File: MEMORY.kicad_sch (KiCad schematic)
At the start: 5 parts, among them U2 ICE40HX8K-BG121, U7 S27KL0641

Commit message: Routing changes, pullups, etc
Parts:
- C21, C22, C26, U2: Source (none) -> ANY
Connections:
- net ~CS1: now also U2.D10 (IOR_154); no longer U2.B11 (IOR_161)
- net ~RESET1: now also U2.B11 (IOR_161); no longer U2.D10 (IOR_154)

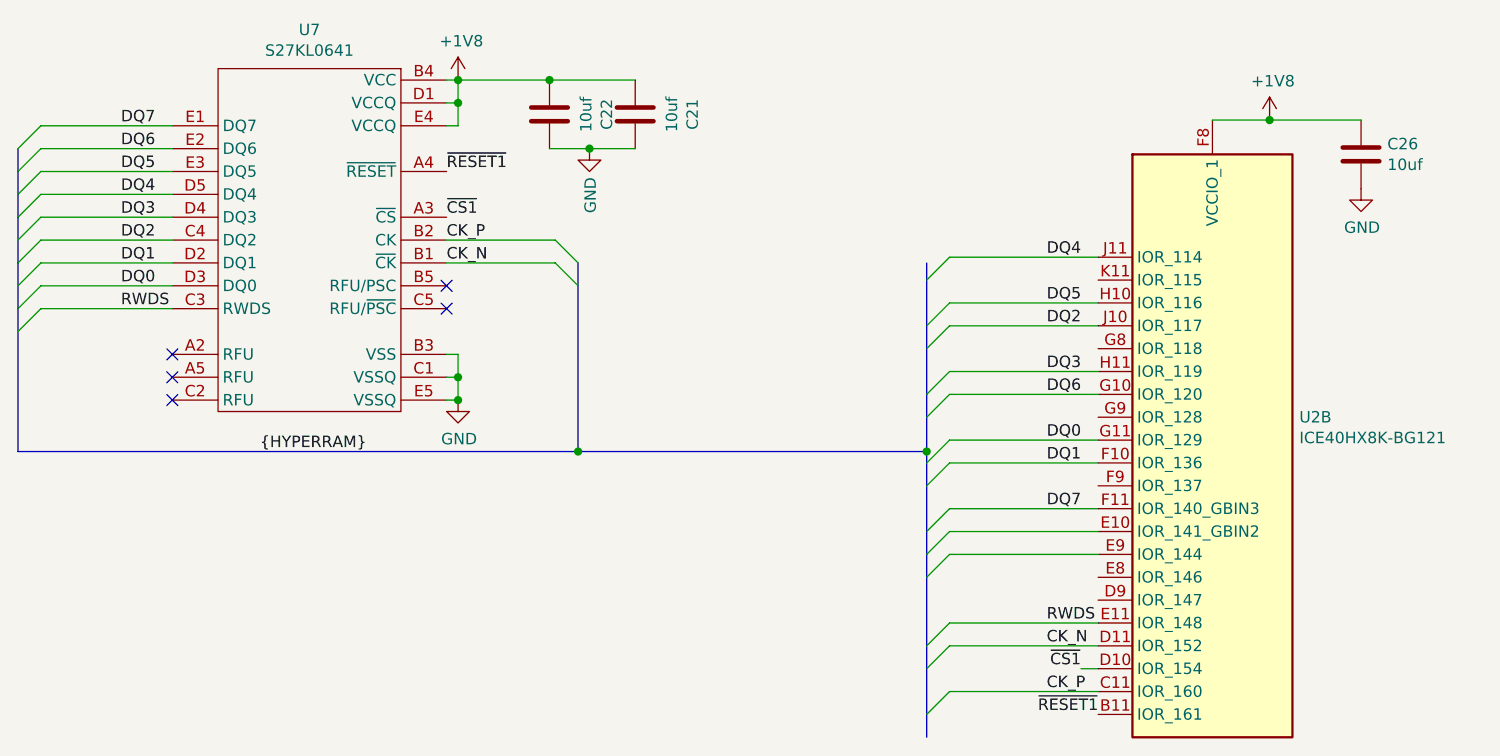
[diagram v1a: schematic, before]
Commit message: Routing cleanup, fix primary transformer
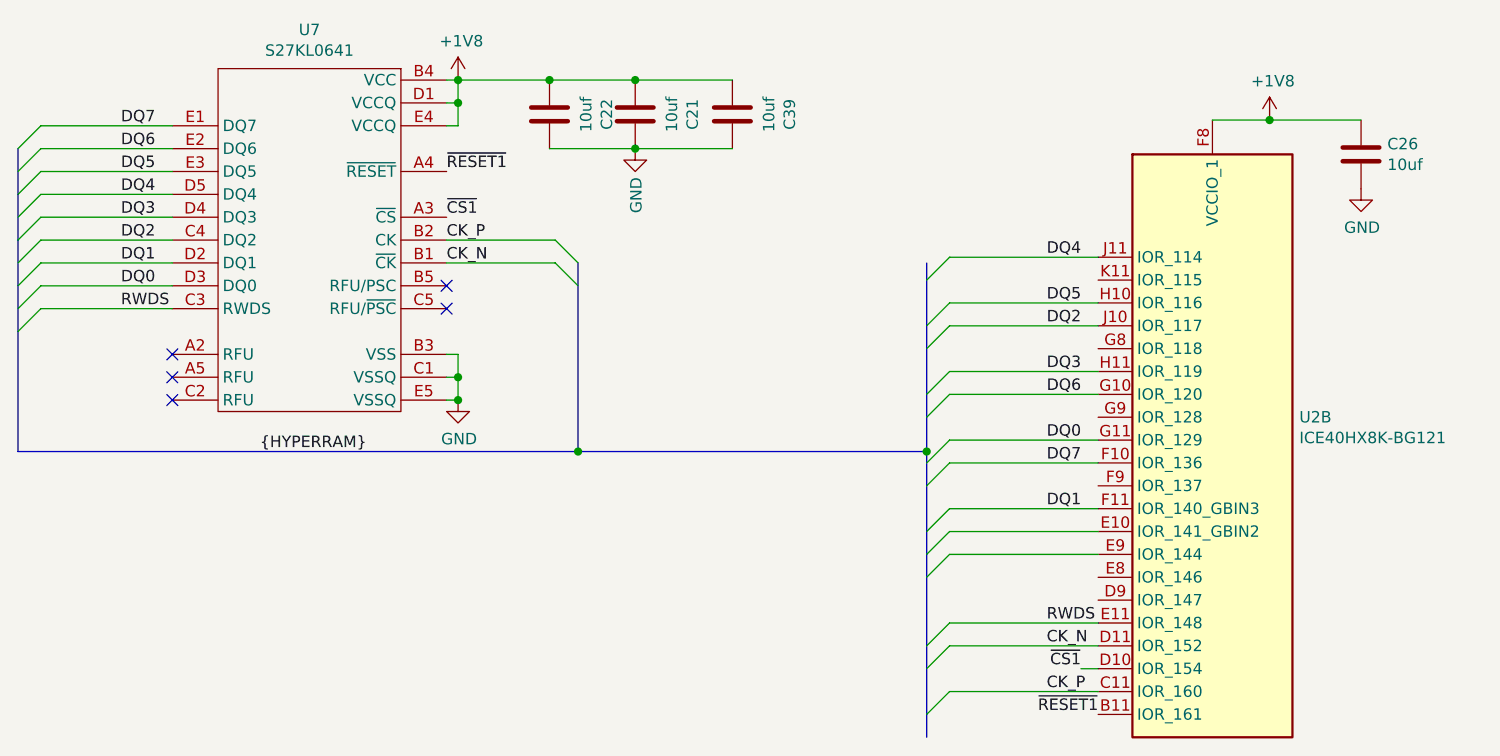
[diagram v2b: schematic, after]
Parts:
- added C39: 10uf, Capacitor_SMD:C_0402_1005Metric, symbol Device:C
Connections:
- net +1V8: now also C39.1
- net DQ1: now also U2.F11 (IOR_140_GBIN3); no longer U2.F10 (IOR_136)
- net DQ7: now also U2.F10 (IOR_136); no longer U2.F11 (IOR_140_GBIN3)
- net GND: now also C39.2
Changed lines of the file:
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@@
   (page 5 7)
   (paper "A4")
+  (title_block
+    (rev "TEST")
+  )
   (bus_alias "HYPERRAM" (members "DQ[7..0]" "RWDS" "~CS" "CK" "~CK" "RFU/PSC" "RFU/~PSC"))
   (junction (at 118.745 57.785))
@@
   (junction (at 118.745 93.345))
   (junction (at 128.905 57.785))
-  (junction (at 133.35 65.405))
+  (junction (at 138.43 57.785))
+  (junction (at 138.43 65.405))
   (junction (at 208.915 62.23))
   (junction (at 132.08 99.06))
   (junction (at 170.815 99.06))
   (no_connect (at 117.475 80.645))
-  (no_connect (at 86.995 90.805))
+  (no_connect (at 86.995 93.345))
   (no_connect (at 117.475 83.185))
   (no_connect (at 86.995 88.265))
-  (no_connect (at 86.995 93.345))
+  (no_connect (at 86.995 90.805))
   (bus_entry (at 69.85 65.405) (size 2.54 -2.54))
   (bus_entry (at 69.85 67.945) (size 2.54 -2.54))
@@
     (stroke (width 0) (type solid) (color 0 0 0 0))
   )
-  (wire (pts (xy 128.905 65.405) (xy 133.35 65.405))
-    (stroke (width 0) (type solid) (color 0 0 0 0))
-  )
-  (wire (pts (xy 133.35 65.405) (xy 138.43 65.405))
+  (wire (pts (xy 128.905 65.405) (xy 138.43 65.405))
+    (stroke (width 0) (type solid) (color 0 0 0 0))
+  )
+  (wire (pts (xy 138.43 57.785) (xy 149.225 57.785))
+    (stroke (width 0) (type solid) (color 0 0 0 0))
+  )
+  (wire (pts (xy 138.43 65.405) (xy 149.225 65.405))
     (stroke (width 0) (type solid) (color 0 0 0 0))
   )
@@
     (stroke (width 0) (type solid) (color 0 0 0 0))
   )
-  (bus (pts (xy 69.85 65.405) (xy 69.85 67.945))
-    (stroke (width 0) (type solid) (color 0 0 0 0))
-  )
-  (bus (pts (xy 69.85 67.945) (xy 69.85 73.025))
-    (stroke (width 0) (type solid) (color 0 0 0 0))
-  )
-  (bus (pts (xy 69.85 73.025) (xy 69.85 78.105))
-    (stroke (width 0) (type solid) (color 0 0 0 0))
-  )
-  (bus (pts (xy 69.85 78.105) (xy 69.85 83.185))
-    (stroke (width 0) (type solid) (color 0 0 0 0))
-  )
-  (bus (pts (xy 69.85 83.185) (xy 69.85 99.06))
+  (bus (pts (xy 69.85 65.405) (xy 69.85 70.485))
+    (stroke (width 0) (type solid) (color 0 0 0 0))
+  )
+  (bus (pts (xy 69.85 70.485) (xy 69.85 75.565))
+    (stroke (width 0) (type solid) (color 0 0 0 0))
+  )
+  (bus (pts (xy 69.85 75.565) (xy 69.85 80.645))
+    (stroke (width 0) (type solid) (color 0 0 0 0))
+  )
+  (bus (pts (xy 69.85 80.645) (xy 69.85 85.725))
+    (stroke (width 0) (type solid) (color 0 0 0 0))
+  )
+  (bus (pts (xy 69.85 85.725) (xy 69.85 99.06))
     (stroke (width 0) (type solid) (color 0 0 0 0))
   )
@@
     (stroke (width 0) (type solid) (color 0 0 0 0))
   )
-  (bus (pts (xy 170.815 85.09) (xy 170.815 92.71))
-    (stroke (width 0) (type solid) (color 0 0 0 0))
-  )
-  (bus (pts (xy 170.815 92.71) (xy 170.815 99.06))
+  (bus (pts (xy 170.815 85.09) (xy 170.815 87.63))
+    (stroke (width 0) (type solid) (color 0 0 0 0))
+  )
+  (bus (pts (xy 170.815 87.63) (xy 170.815 95.25))
+    (stroke (width 0) (type solid) (color 0 0 0 0))
+  )
+  (bus (pts (xy 170.815 95.25) (xy 170.815 99.06))
     (stroke (width 0) (type solid) (color 0 0 0 0))
   )
@@
     (stroke (width 0) (type solid) (color 0 0 0 0))
   )
-  (bus (pts (xy 170.815 110.49) (xy 170.815 113.03))
-    (stroke (width 0) (type solid) (color 0 0 0 0))
-  )
-  (bus (pts (xy 170.815 113.03) (xy 170.815 123.19))
-    (stroke (width 0) (type solid) (color 0 0 0 0))
-  )
-  (bus (pts (xy 170.815 123.19) (xy 170.815 130.81))
+  (bus (pts (xy 170.815 110.49) (xy 170.815 120.65))
+    (stroke (width 0) (type solid) (color 0 0 0 0))
+  )
+  (bus (pts (xy 170.815 120.65) (xy 170.815 128.27))
+    (stroke (width 0) (type solid) (color 0 0 0 0))
+  )
+  (bus (pts (xy 170.815 128.27) (xy 170.815 130.81))
     (stroke (width 0) (type solid) (color 0 0 0 0))
   )
@@
     (effects (font (size 1.27 1.27)) (justify left bottom))
   )
-  (label "DQ1" (at 184.15 100.33 0)
-    (effects (font (size 1.27 1.27)) (justify left bottom))
-  )
-  (label "DQ7" (at 184.15 105.41 0)
+  (label "DQ7" (at 184.15 100.33 0)
+    (effects (font (size 1.27 1.27)) (justify left bottom))
+  )
+  (label "DQ1" (at 184.15 105.41 0)
     (effects (font (size 1.27 1.27)) (justify left bottom))
   )
@@
     )
   )
-  (symbol (lib_id "power:GND") (at 133.35 65.405 0) (unit 1)
-    (property "Reference" "#PWR0148" (id 0) (at 133.35 71.755 0)
-      (effects (font (size 1.27 1.27)) hide)
-    )
-    (property "Value" "GND" (id 1) (at 133.4643 68.5801 90)
+  (symbol (lib_id "power:GND") (at 138.43 65.405 0) (unit 1)
+    (property "Reference" "#PWR0148" (id 0) (at 138.43 71.755 0)
+      (effects (font (size 1.27 1.27)) hide)
+    )
+    (property "Value" "GND" (id 1) (at 138.5443 68.5801 90)
       (effects (font (size 1.27 1.27)) (justify right))
     )
-    (property "Footprint" "" (id 2) (at 133.35 65.405 0)
-      (effects (font (size 1.27 1.27)) hide)
-    )
-    (property "Datasheet" "" (id 3) (at 133.35 65.405 0)
+    (property "Footprint" "" (id 2) (at 138.43 65.405 0)
+      (effects (font (size 1.27 1.27)) hide)
+    )
+    (property "Datasheet" "" (id 3) (at 138.43 65.405 0)
       (effects (font (size 1.27 1.27)) hide)
     )
@@
       (effects (font (size 1.27 1.27)) hide)
     )
+  )
+  (symbol (lib_id "Device:C") (at 149.225 61.595 0) (unit 1)
+    (property "Reference" "C39" (id 0) (at 155.5942 61.595 90))
+    (property "Value" "10uf" (id 1) (at 153.2955 61.595 90))
+    (property "Footprint" "Capacitor_SMD:C_0402_1005Metric" (id 2) (at 150.1902 65.405 0)
+      (effects (font (size 1.27 1.27)) hide)
+    )
+    (property "Datasheet" "~" (id 3) (at 149.225 61.595 0)
+      (effects (font (size 1.27 1.27)) hide)
+    )
+    (property "Source" "ANY" (id 4) (at 149.225 61.595 0)
+      (effects (font (size 1.27 1.27)) hide)
+    )

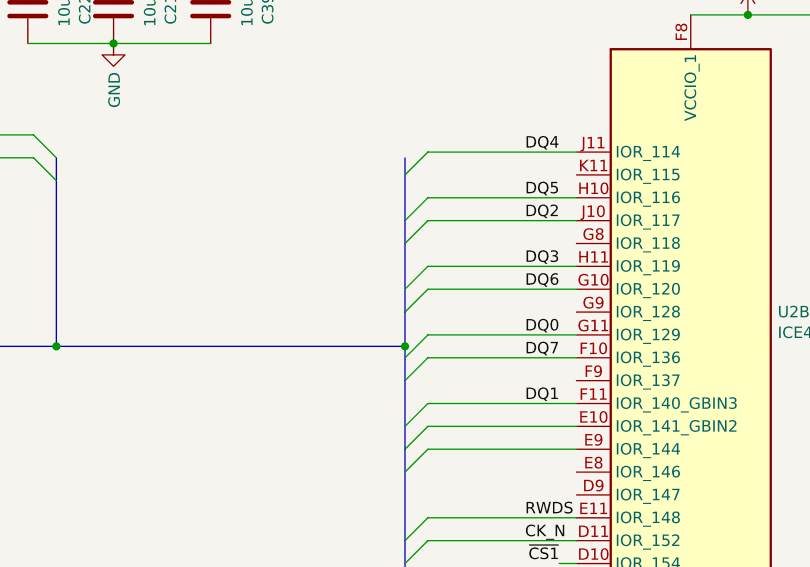
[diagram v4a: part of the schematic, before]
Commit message: Add missing detection resistor
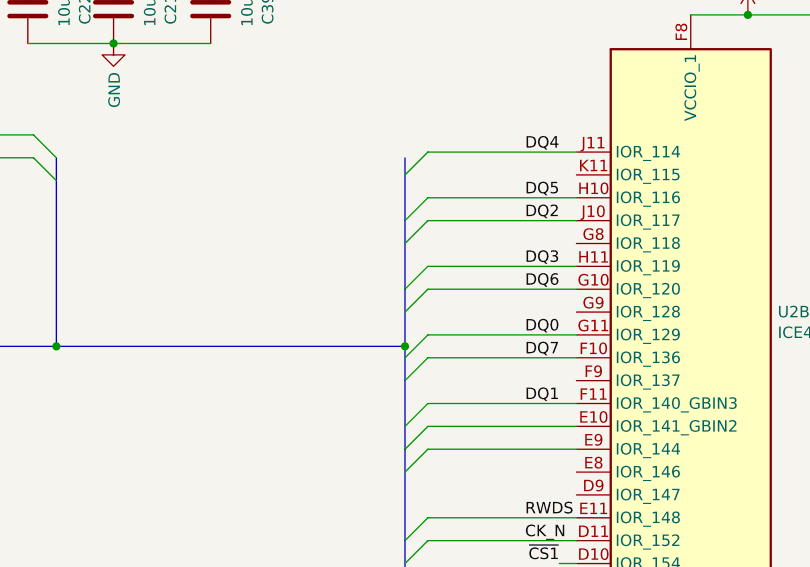
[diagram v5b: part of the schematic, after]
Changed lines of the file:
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@@
-(kicad_sch (version 20200608) (host eeschema "5.99.0-unknown-60915fb~101~ubuntu20.04.1")
+(kicad_sch (version 20200608) (host eeschema "5.99.0-unknown-e164269~101~ubuntu20.04.1")
   (page 1 7)
   (paper "A4")
@@
   (junction (at 132.08 99.06))
   (junction (at 170.815 99.06))
+  (no_connect (at 86.995 93.345))
+  (no_connect (at 117.475 80.645))
+  (no_connect (at 117.475 83.185))
+  (no_connect (at 86.995 90.805))
   (no_connect (at 86.995 88.265))
-  (no_connect (at 117.475 80.645))
-  (no_connect (at 86.995 93.345))
-  (no_connect (at 86.995 90.805))
-  (no_connect (at 117.475 83.185))
   (bus_entry (at 69.85 65.405) (size 2.54 -2.54))
   (bus_entry (at 69.85 67.945) (size 2.54 -2.54))
@@
     (stroke (width 0) (type solid) (color 0 0 0 0))
   )
-  (bus (pts (xy 170.815 85.09) (xy 170.815 87.63))
-    (stroke (width 0) (type solid) (color 0 0 0 0))
-  )
-  (bus (pts (xy 170.815 87.63) (xy 170.815 95.25))
-    (stroke (width 0) (type solid) (color 0 0 0 0))
-  )
-  (bus (pts (xy 170.815 95.25) (xy 170.815 99.06))
-    (stroke (width 0) (type solid) (color 0 0 0 0))
-  )
+  (bus (pts (xy 170.815 85.09) (xy 170.815 92.71))
+    (stroke (width 0) (type solid) (color 0 0 0 0))
+  )
+  (bus (pts (xy 170.815 92.71) (xy 170.815 99.06))
+    (stroke (width 0) (type solid) (color 0 0 0 0))
+  )

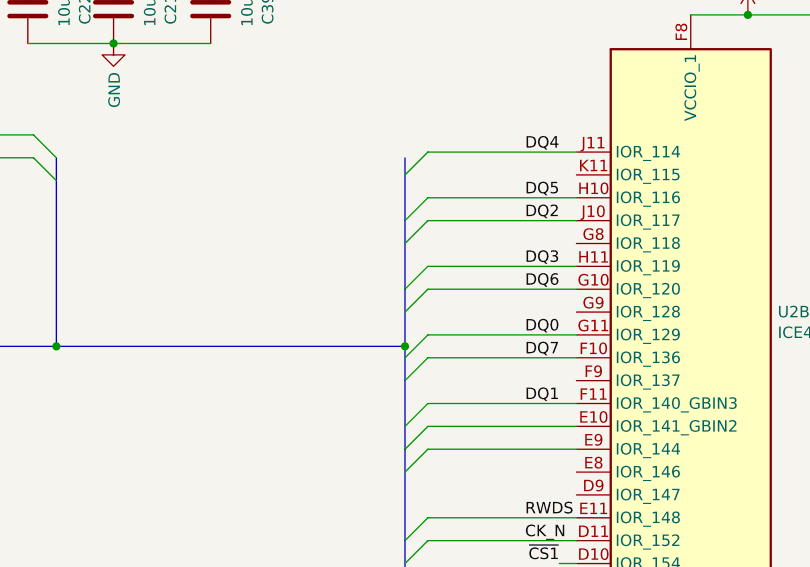
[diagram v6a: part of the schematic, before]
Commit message: Fix SOT-89-3 footprint
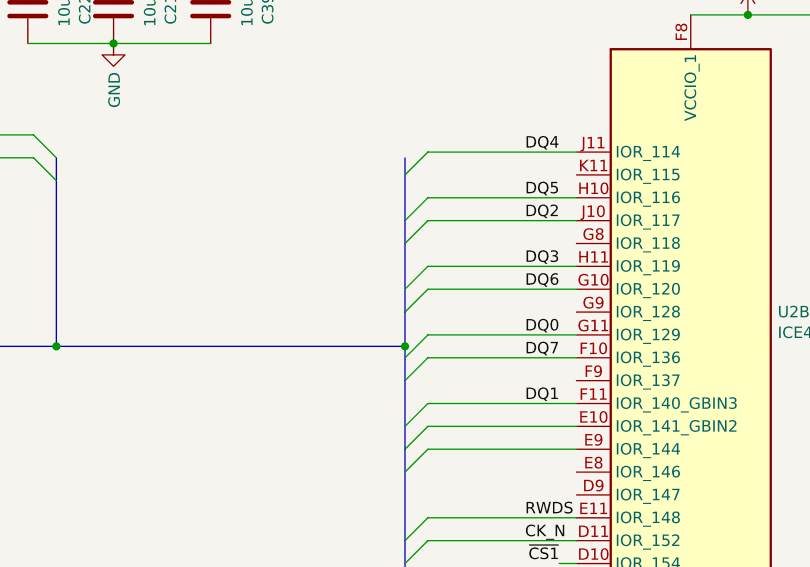
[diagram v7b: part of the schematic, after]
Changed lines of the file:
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@@
-(kicad_sch (version 20200618) (host eeschema "5.99.0-unknown-b48a627~101~ubuntu20.04.1")
+(kicad_sch (version 20200618) (host eeschema "5.99.0-unknown-19b7755~101~ubuntu20.04.1")
   (page 1 7)
   (paper "A4")
@@
   (junction (at 132.08 99.06) (diameter 0) (color 0 0 0 0))
   (junction (at 170.815 99.06) (diameter 0) (color 0 0 0 0))
+  (no_connect (at 117.475 83.185))
   (no_connect (at 86.995 88.265))
+  (no_connect (at 86.995 93.345))
+  (no_connect (at 117.475 80.645))
   (no_connect (at 86.995 90.805))
-  (no_connect (at 117.475 80.645))
-  (no_connect (at 86.995 93.345))
-  (no_connect (at 117.475 83.185))
   (bus_entry (at 69.85 65.405) (size 2.54 -2.54)
     (stroke (width 0.1524) (type solid) (color 0 0 0 0))
@@
     (stroke (width 0) (type solid) (color 0 0 0 0))
   )
-  (bus (pts (xy 170.815 85.09) (xy 170.815 92.71))
-    (stroke (width 0) (type solid) (color 0 0 0 0))
-  )
-  (bus (pts (xy 170.815 92.71) (xy 170.815 99.06))
-    (stroke (width 0) (type solid) (color 0 0 0 0))
-  )
+  (bus (pts (xy 170.815 85.09) (xy 170.815 87.63))
+    (stroke (width 0) (type solid) (color 0 0 0 0))
+  )
+  (bus (pts (xy 170.815 87.63) (xy 170.815 95.25))
+    (stroke (width 0) (type solid) (color 0 0 0 0))
+  )
+  (bus (pts (xy 170.815 95.25) (xy 170.815 99.06))
+    (stroke (width 0) (type solid) (color 0 0 0 0))
+  )

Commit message: Swap low voltage caps, remove hv side LC filter
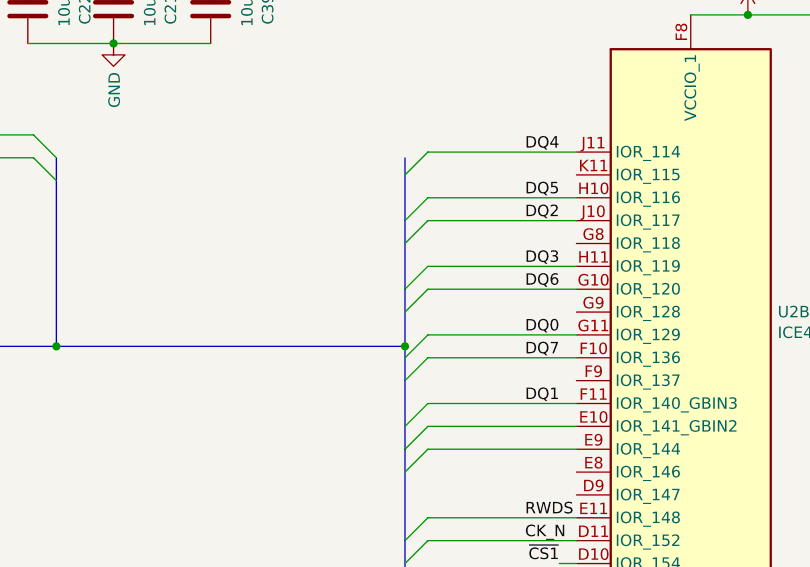
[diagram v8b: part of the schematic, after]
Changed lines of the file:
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@@
-(kicad_sch (version 20200618) (host eeschema "5.99.0-unknown-19b7755~101~ubuntu20.04.1")
+(kicad_sch (version 20200618) (host eeschema "5.99.0-unknown-af8f05d~101~ubuntu20.04.1")
   (page 1 7)
   (paper "A4")
@@
   (junction (at 132.08 99.06) (diameter 0) (color 0 0 0 0))
   (junction (at 170.815 99.06) (diameter 0) (color 0 0 0 0))
+  (no_connect (at 86.995 88.265))
   (no_connect (at 117.475 83.185))
-  (no_connect (at 86.995 88.265))
+  (no_connect (at 117.475 80.645))
   (no_connect (at 86.995 93.345))
-  (no_connect (at 117.475 80.645))
   (no_connect (at 86.995 90.805))
   (bus_entry (at 69.85 65.405) (size 2.54 -2.54)
@@
     (stroke (width 0) (type solid) (color 0 0 0 0))
   )
-  (bus (pts (xy 170.815 85.09) (xy 170.815 87.63))
-    (stroke (width 0) (type solid) (color 0 0 0 0))
-  )
-  (bus (pts (xy 170.815 87.63) (xy 170.815 95.25))
-    (stroke (width 0) (type solid) (color 0 0 0 0))
-  )
-  (bus (pts (xy 170.815 95.25) (xy 170.815 99.06))
-    (stroke (width 0) (type solid) (color 0 0 0 0))
-  )
+  (bus (pts (xy 170.815 85.09) (xy 170.815 92.71))
+    (stroke (width 0) (type solid) (color 0 0 0 0))
+  )
+  (bus (pts (xy 170.815 92.71) (xy 170.815 99.06))
+    (stroke (width 0) (type solid) (color 0 0 0 0))
+  )
